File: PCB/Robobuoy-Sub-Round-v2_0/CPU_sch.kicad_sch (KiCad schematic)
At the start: 38 parts, among them J101 Prog, Q101 AO3400A, SW101 ~{RESET}, SW102 MODE, U101 ESP32-WROOM-32E_(visible_peri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, U102 LSM303AGRTR, U103 USBLC6-4SC6

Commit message: PCP's finsehd for production.
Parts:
- J101: LCSC (none) -> C65114
- SW101: now in the parts list
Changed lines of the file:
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@@
 		(unit 1)
 		(exclude_from_sim no)
-		(in_bom no)
+		(in_bom yes)
 		(on_board yes)
 		(dnp yes)
@@
 			(at 43.18 27.94 0)
 			(effects
+				(font
+					(size 1.27 1.27)
+				)
+				(hide yes)
+			)
+		)
+		(property "LCSC" "C65114"
+			(at 43.18 27.94 0)
+			(effects

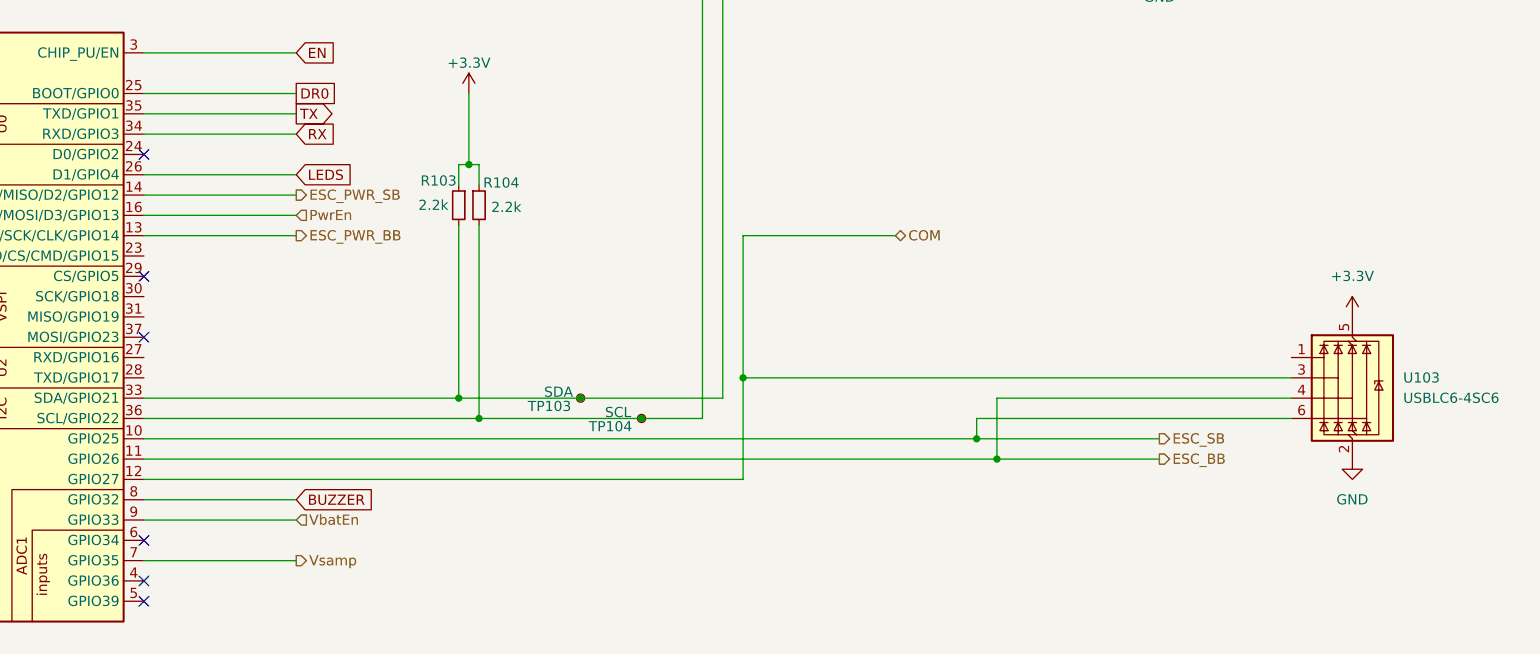
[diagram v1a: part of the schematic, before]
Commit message: Serial comms working now
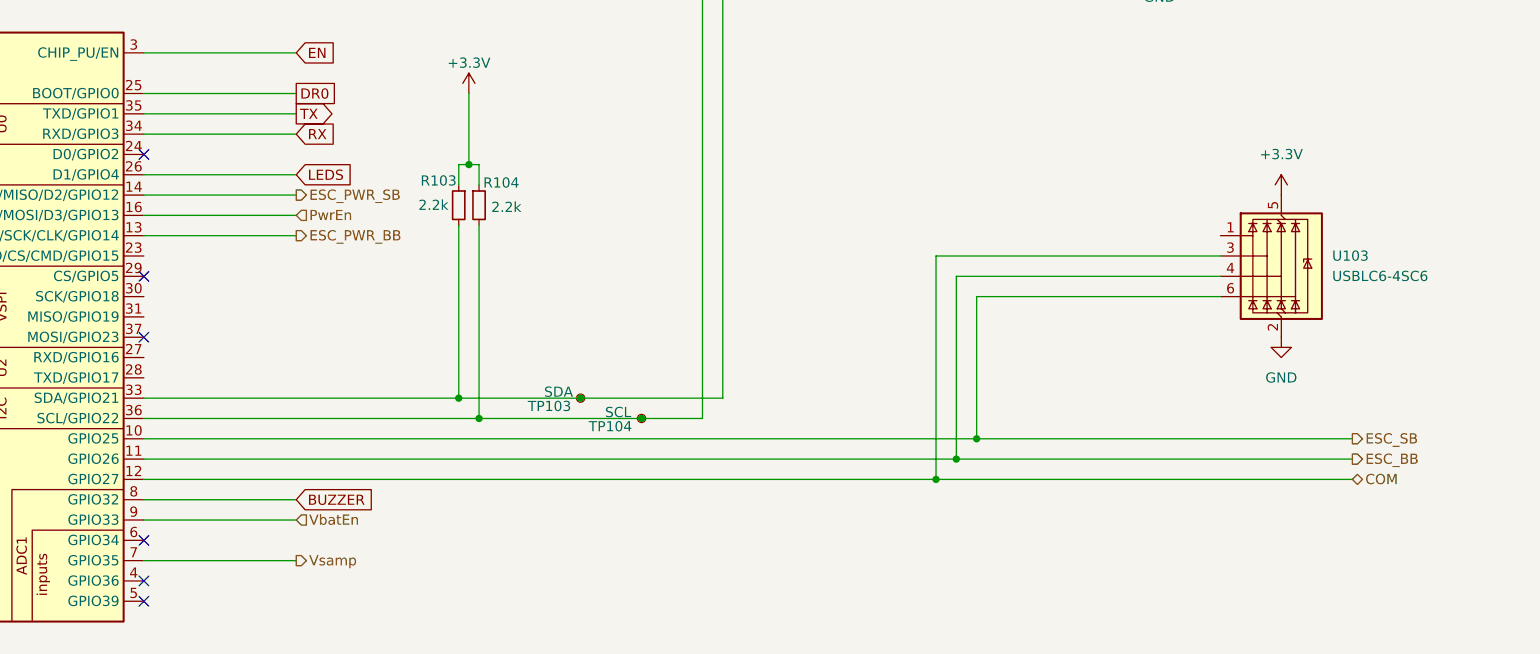
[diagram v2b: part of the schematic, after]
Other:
- moved on the sheet: U103
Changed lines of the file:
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@@
 	)
 	(junction
+		(at 297.18 129.54)
+		(diameter 0)
+		(color 0 0 0 0)
+	)
+	(junction
 		(at 120.65 262.89)
 		(diameter 0)
@@
 	)
 	(junction
-		(at 273.05 116.84)
-		(diameter 0)
-		(color 0 0 0 0)
-	)
-	(junction
 		(at 170.18 152.4)
 		(diameter 0)
@@
 	)
 	(junction
-		(at 304.8 127)
-		(diameter 0)
-		(color 0 0 0 0)
-	)
-	(junction
 		(at 147.32 257.81)
 		(diameter 0)
@@
 	)
 	(junction
+		(at 299.72 127)
+		(diameter 0)
+		(color 0 0 0 0)
+	)
+	(junction
 		(at 95.25 262.89)
 		(diameter 0)
@@
 	(wire
 		(pts
-			(xy 304.8 127) (xy 325.12 127)
-		)
-		(stroke
-			(width 0)
-			(type default)
-		)
-	)
-	(wire
-		(pts
 			(xy 120.65 262.89) (xy 128.27 262.89)
 		)
@@
 	(wire
 		(pts
-			(xy 304.8 119.38) (xy 304.8 127)
+			(xy 299.72 104.14) (xy 299.72 127)
 		)
 		(stroke
@@
 	(wire
 		(pts
+			(xy 297.18 129.54) (xy 349.25 129.54)
+		)
+		(stroke
+			(width 0)
+			(type default)
+		)
+	)
+	(wire
+		(pts
 			(xy 342.9 49.53) (xy 345.44 49.53)
 		)
@@
 	(wire
 		(pts
-			(xy 273.05 99.06) (xy 273.05 116.84)
-		)
-		(stroke
-			(width 0)
-			(type default)
-		)
-	)
-	(wire
-		(pts
 			(xy 165.1 152.4) (xy 165.1 149.86)
 		)
@@
 	(wire
 		(pts
-			(xy 198.12 129.54) (xy 273.05 129.54)
-		)
-		(stroke
-			(width 0)
-			(type default)
-		)
-	)
-	(wire
-		(pts
 			(xy 110.49 262.89) (xy 120.65 262.89)
 		)
@@
 	(wire
 		(pts
-			(xy 302.26 124.46) (xy 325.12 124.46)
+			(xy 302.26 124.46) (xy 349.25 124.46)
 		)
 		(stroke
@@
 	(wire
 		(pts
-			(xy 302.26 121.92) (xy 341.63 121.92)
+			(xy 302.26 106.68) (xy 332.74 106.68)
 		)
 		(stroke
@@
 	(wire
 		(pts
-			(xy 273.05 129.54) (xy 273.05 116.84)
+			(xy 39.37 243.84) (xy 39.37 246.38)
 		)
 		(stroke
@@
 	(wire
 		(pts
-			(xy 39.37 243.84) (xy 39.37 246.38)
+			(xy 147.32 262.89) (xy 154.94 262.89)
 		)
 		(stroke
@@
 		)
 	)
-	(wire
+	(polyline
 		(pts
-			(xy 147.32 262.89) (xy 154.94 262.89)
+			(xy 80.01 281.94) (xy 16.51 281.94)
 		)
 		(stroke
@@
 		)
 	)
-	(polyline
+	(wire
 		(pts
-			(xy 80.01 281.94) (xy 16.51 281.94)
+			(xy 243.84 243.84) (xy 243.84 245.11)
 		)
 		(stroke
@@
 	(wire
 		(pts
-			(xy 243.84 243.84) (xy 243.84 245.11)
+			(xy 297.18 101.6) (xy 297.18 129.54)
 		)
 		(stroke
@@
 	(wire
 		(pts
-			(xy 302.26 121.92) (xy 302.26 124.46)
+			(xy 302.26 106.68) (xy 302.26 124.46)
 		)
 		(stroke
@@
 	(wire
 		(pts
-			(xy 341.63 116.84) (xy 273.05 116.84)
+			(xy 332.74 101.6) (xy 297.18 101.6)
 		)
 		(stroke
@@
 	(wire
 		(pts
+			(xy 299.72 127) (xy 349.25 127)
+		)
+		(stroke
+			(width 0)
+			(type default)
+		)
+	)
+	(wire
+		(pts
 			(xy 295.91 26.67) (xy 295.91 29.21)
 		)
@@
 	(wire
 		(pts
-			(xy 304.8 119.38) (xy 341.63 119.38)
+			(xy 299.72 104.14) (xy 332.74 104.14)
 		)
 		(stroke
@@
 	(wire
 		(pts
-			(xy 198.12 127) (xy 304.8 127)
+			(xy 198.12 127) (xy 299.72 127)
 		)
 		(stroke
@@
 	(wire
 		(pts
-			(xy 273.05 99.06) (xy 292.1 99.06)
+			(xy 198.12 129.54) (xy 297.18 129.54)
 		)
 		(stroke
@@
 	(hierarchical_label "COM"
 		(shape bidirectional)
-		(at 292.1 99.06 0)
+		(at 349.25 129.54 0)
 		(effects
 			(font
@@
 	(hierarchical_label "ESC_SB"
 		(shape output)
-		(at 325.12 124.46 0)
+		(at 349.25 124.46 0)
 		(effects
 			(font
@@
 	(hierarchical_label "ESC_BB"
 		(shape output)
-		(at 325.12 127 0)
+		(at 349.25 127 0)
 		(effects
 			(font
@@
 	(symbol
 		(lib_id "power:+3.3V")
-		(at 349.25 109.22 0)
+		(at 340.36 93.98 0)
 		(mirror y)
 		(unit 1)
@@
 		(fields_autoplaced yes)
 		(property "Reference" "#PWR0125"
-			(at 349.25 113.03 0)
+			(at 340.36 97.79 0)
 			(effects
 				(font
@@
 		)
 		(property "Value" "+3.3V"
-			(at 349.25 104.14 0)
+			(at 340.36 88.9 0)
 			(effects
 				(font
@@
 		)
 		(property "Footprint" ""
-			(at 349.25 109.22 0)
+			(at 340.36 93.98 0)
 			(effects
 				(font
@@
 		)
 		(property "Datasheet" ""
-			(at 349.25 109.22 0)
+			(at 340.36 93.98 0)
 			(effects
 				(font
@@
 		)
 		(property "Description" ""
-			(at 349.25 109.22 0)
+			(at 340.36 93.98 0)
 			(effects
 				(font
@@
 	(symbol
 		(lib_id "power:GND")
-		(at 349.25 127 0)
+		(at 340.36 111.76 0)
 		(mirror y)
 		(unit 1)
@@
 		(fields_autoplaced yes)
 		(property "Reference" "#PWR0126"
-			(at 349.25 133.35 0)
+			(at 340.36 118.11 0)
 			(effects
 				(font
@@
 		)
 		(property "Value" "GND"
-			(at 349.25 132.08 0)
+			(at 340.36 116.84 0)
 			(effects
 				(font
@@
 		)
 		(property "Footprint" ""
-			(at 349.25 127 0)
+			(at 340.36 111.76 0)
 			(effects
 				(font
@@
 		)
 		(property "Datasheet" ""
-			(at 349.25 127 0)
+			(at 340.36 111.76 0)
 			(effects
 				(font
@@
 		)
 		(property "Description" ""
-			(at 349.25 127 0)
+			(at 340.36 111.76 0)
 			(effects
 				(font
@@
 	(symbol
 		(lib_id "Power_Protection:USBLC6-4SC6")
-		(at 349.25 116.84 0)
+		(at 340.36 101.6 0)
 		(unit 1)
 		(exclude_from_sim no)
@@
 		(fields_autoplaced yes)
 		(property "Reference" "U103"
-			(at 355.6 116.8399 0)
+			(at 346.71 101.5999 0)
 			(effects
 				(font
@@
 		)
 		(property "Value" "USBLC6-4SC6"
-			(at 355.6 119.3799 0)
+			(at 346.71 104.1399 0)
 			(effects
 				(font
@@
 		)
 		(property "Footprint" "Package_TO_SOT_SMD:SOT-23-6"
-			(at 351.79 127 0)
+			(at 342.9 111.76 0)
 			(effects
 				(font
@@
 		)
 		(property "Datasheet" "https://www.st.com/resource/en/datasheet/usblc6-4.pdf"
-			(at 351.79 129.54 0)
+			(at 342.9 114.3 0)
 			(effects
 				(font
@@
 		)
 		(property "Description" "Very low capacitance ESD protection diode, 4 data-line, SOT-23-6"
-			(at 349.25 116.84 0)
+			(at 340.36 101.6 0)
 			(effects
 				(font
@@
 		)
 		(property "JLCS" ""
-			(at 349.25 116.84 0)
+			(at 340.36 101.6 0)
 			(effects
 				(font
@@
 		)
 		(property "LCSC" "C5197386"
-			(at 355.6 116.8399 0)
+			(at 346.71 101.5999 0)
 			(effects
 				(font
@@
 		)
 		(property "Field5" ""
-			(at 349.25 116.84 0)
+			(at 340.36 101.6 0)
 			(effects
 				(font
@@
 		)
 		(property "Type" ""
-			(at 349.25 116.84 0)
+			(at 340.36 101.6 0)
 			(effects
 				(font
